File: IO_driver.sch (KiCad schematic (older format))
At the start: 9 parts, among them J2 BNC, U7 74LVC2T45DC

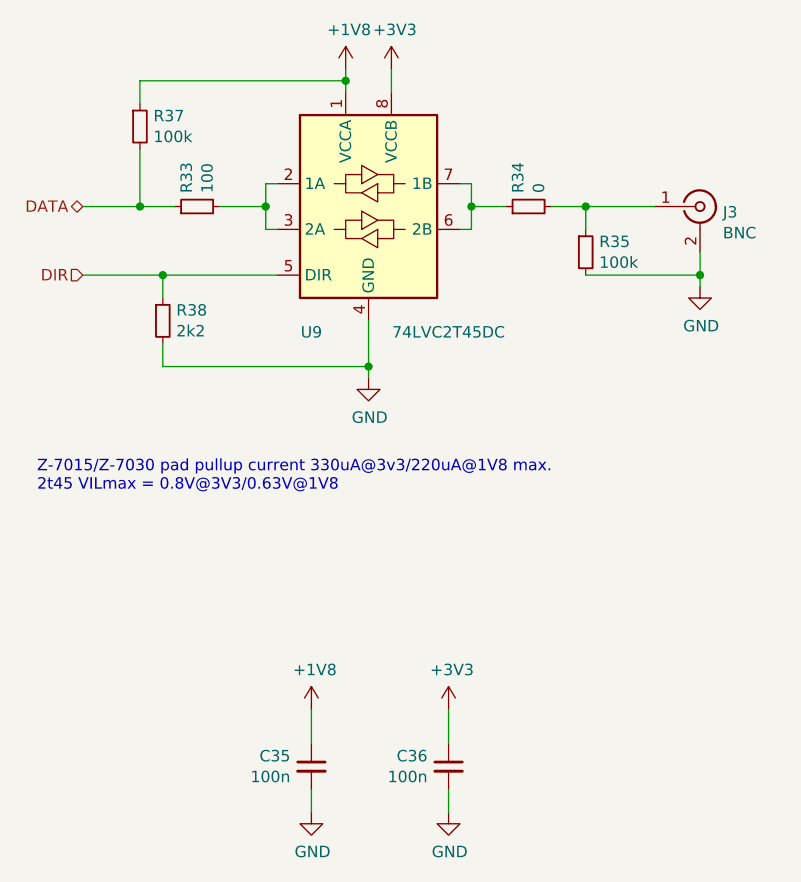
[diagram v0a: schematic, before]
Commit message: reannotated for merging with te0715 development board
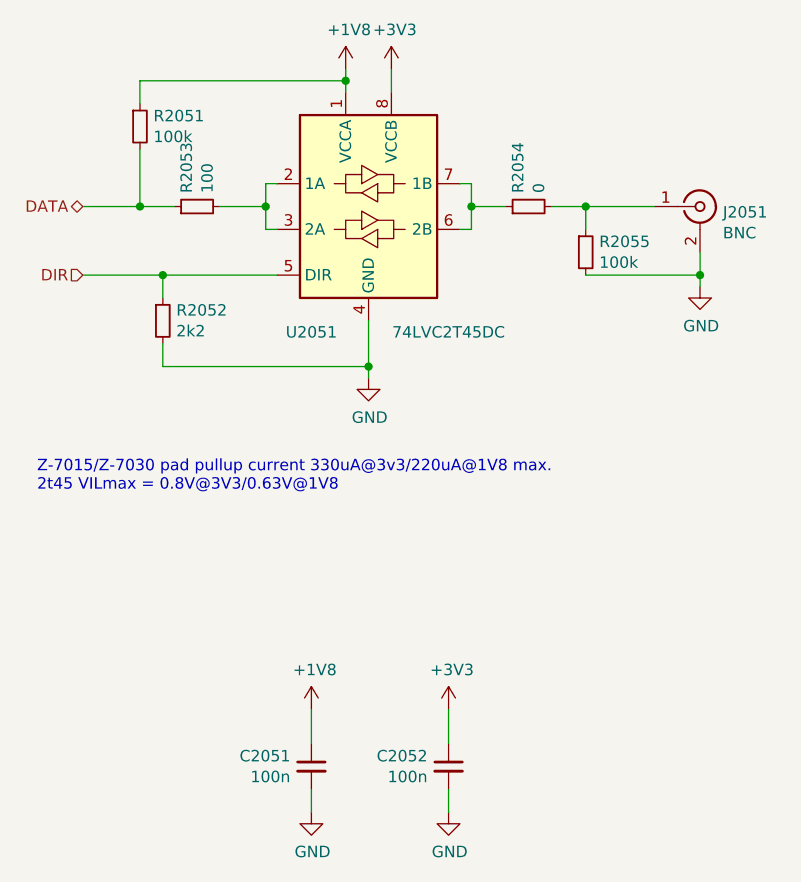
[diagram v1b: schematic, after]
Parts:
- renumbered C33 to C2001, C34 to C2002, J2 to J2001, R29 to R2001, R36 to R2002, R30 to R2003, R31 to R2004, R32 to R2005, U7 to U2001
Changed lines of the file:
@@
 $Descr A4 11693 8268
 encoding utf-8
-Sheet 5 6
+Sheet 6 6
 Title ""
 Date ""
@@
 AR Path="/60F26603" Ref="R?"  Part="1"
 AR Path="/60DB2574/60F26603" Ref="R?"  Part="1"
-AR Path="/60DB2574/60EF9F81/60F26603" Ref="R31"  Part="1"
-AR Path="/60DB2574/60E556C7/60F26603" Ref="R34"  Part="1"
-F 0 "R34" H 5259 1896 50  0000 L CNN
+AR Path="/60DB2574/60EF9F81/60F26603" Ref="R2004"  Part="1"
+AR Path="/60DB2574/60E556C7/60F26603" Ref="R2054"  Part="1"
+F 0 "R2054" H 5259 1896 50  0000 L CNN
 F 1 "0" H 5259 1805 50  0000 L CNN
 F 2 "Resistor_SMD:R_0603_1608Metric" H 5200 1850 50  0001 C CNN
@@
 AR Path="/60F26C82" Ref="R?"  Part="1"
 AR Path="/60DB2574/60F26C82" Ref="R?"  Part="1"
-AR Path="/60DB2574/60EF9F81/60F26C82" Ref="R30"  Part="1"
-AR Path="/60DB2574/60E556C7/60F26C82" Ref="R33"  Part="1"
-F 0 "R33" H 3809 1896 50  0000 L CNN
+AR Path="/60DB2574/60EF9F81/60F26C82" Ref="R2003"  Part="1"
+AR Path="/60DB2574/60E556C7/60F26C82" Ref="R2053"  Part="1"
+F 0 "R2053" H 3809 1896 50  0000 L CNN
 F 1 "100" H 3809 1805 50  0000 L CNN
 F 2 "Resistor_SMD:R_0603_1608Metric" H 3750 1850 50  0001 C CNN
@@
 	3250 2150 3600 2150
 $Comp
-L Device:C_Small C33
+L Device:C_Small C2001
 U 1 1 60F2A5CB
 P 4250 4300
-AR Path="/60DB2574/60EF9F81/60F2A5CB" Ref="C33"  Part="1"
-AR Path="/60DB2574/60E556C7/60F2A5CB" Ref="C35"  Part="1"
-F 0 "C35" H 4342 4346 50  0000 L CNN
+AR Path="/60DB2574/60EF9F81/60F2A5CB" Ref="C2001"  Part="1"
+AR Path="/60DB2574/60E556C7/60F2A5CB" Ref="C2051"  Part="1"
+F 0 "C2051" H 4342 4346 50  0000 L CNN
 F 1 "100n" H 4342 4255 50  0000 L CNN
 F 2 "Capacitor_SMD:C_0402_1005Metric" H 4250 4300 50  0001 C CNN
@@
 	4250 4400 4250 4500
 $Comp
-L Device:C_Small C34
+L Device:C_Small C2002
 U 1 1 60F2C544
 P 4850 4300
-AR Path="/60DB2574/60EF9F81/60F2C544" Ref="C34"  Part="1"
-AR Path="/60DB2574/60E556C7/60F2C544" Ref="C36"  Part="1"
-F 0 "C36" H 4942 4346 50  0000 L CNN
+AR Path="/60DB2574/60EF9F81/60F2C544" Ref="C2002"  Part="1"
+AR Path="/60DB2574/60E556C7/60F2C544" Ref="C2052"  Part="1"
+F 0 "C2052" H 4942 4346 50  0000 L CNN
 F 1 "100n" H 4942 4255 50  0000 L CNN
 F 2 "Capacitor_SMD:C_0402_1005Metric" H 4850 4300 50  0001 C CNN
@@
 AR Path="/612B1274/611783BC/60E51E93" Ref="J?"  Part="1"
 AR Path="/612B1274/611E90A8/60E51E93" Ref="J?"  Part="1"
-AR Path="/60DB2574/60EF9F81/60E51E93" Ref="J2"  Part="1"
-AR Path="/60DB2574/60E556C7/60E51E93" Ref="J3"  Part="1"
-F 0 "J3" H 6050 1825 50  0000 L CNN
+AR Path="/60DB2574/60EF9F81/60E51E93" Ref="J2001"  Part="1"
+AR Path="/60DB2574/60E556C7/60E51E93" Ref="J2051"  Part="1"
+F 0 "J2051" H 6050 1825 50  0000 L CNN
 F 1 "BNC" H 6050 1734 50  0000 L CNN
 F 2 "proj_footprints:BNC_Molex_0731713150" H 5950 1850 50  0001 C CNN
@@
 AR Path="/60F05839" Ref="R?"  Part="1"
 AR Path="/60DB2574/60F05839" Ref="R?"  Part="1"
-AR Path="/60DB2574/60EF9F81/60F05839" Ref="R32"  Part="1"
-AR Path="/60DB2574/60E556C7/60F05839" Ref="R35"  Part="1"
-F 0 "R35" H 5509 2096 50  0000 L CNN
+AR Path="/60DB2574/60EF9F81/60F05839" Ref="R2005"  Part="1"
+AR Path="/60DB2574/60E556C7/60F05839" Ref="R2055"  Part="1"
+F 0 "R2055" H 5509 2096 50  0000 L CNN
 F 1 "100k" H 5509 2005 50  0000 L CNN
 F 2 "Resistor_SMD:R_0603_1608Metric" H 5450 2050 50  0001 C CNN
@@
 Z-7015/Z-7030 pad pullup current 330uA@3v3/220uA@1V8 max.\n2t45 VILmax = 0.8V@3V3/0.63V@1V8
 $Comp
-L Logic_LevelTranslator:74LVC2T45DC U7
+L Logic_LevelTranslator:74LVC2T45DC U2001
 U 1 1 60E41AAA
 P 4500 1850
-AR Path="/60DB2574/60EF9F81/60E41AAA" Ref="U7"  Part="1"
-AR Path="/60DB2574/60E556C7/60E41AAA" Ref="U9"  Part="1"
-F 0 "U9" H 4250 1300 50  0000 C CNN
+AR Path="/60DB2574/60EF9F81/60E41AAA" Ref="U2001"  Part="1"
+AR Path="/60DB2574/60E556C7/60E41AAA" Ref="U2051"  Part="1"
+F 0 "U2051" H 4250 1300 50  0000 C CNN
 F 1 "74LVC2T45DC" H 4850 1300 50  0000 C CNN
 F 2 "Package_SO:VSSOP-8_2.3x2mm_P0.5mm" H 4500 1000 50  0001 C CNN
@@
 AR Path="/60E4921E" Ref="R?"  Part="1"
 AR Path="/60DB2574/60E4921E" Ref="R?"  Part="1"
-AR Path="/60DB2574/60EF9F81/60E4921E" Ref="R36"  Part="1"
-AR Path="/60DB2574/60E556C7/60E4921E" Ref="R38"  Part="1"
-F 0 "R38" H 3659 2396 50  0000 L CNN
+AR Path="/60DB2574/60EF9F81/60E4921E" Ref="R2002"  Part="1"
+AR Path="/60DB2574/60E556C7/60E4921E" Ref="R2052"  Part="1"
+F 0 "R2052" H 3659 2396 50  0000 L CNN
 F 1 "2k2" H 3659 2305 50  0000 L CNN
 F 2 "Resistor_SMD:R_0603_1608Metric" H 3600 2350 50  0001 C CNN
@@
 AR Path="/60E49E8E" Ref="R?"  Part="1"
 AR Path="/60DB2574/60E49E8E" Ref="R?"  Part="1"
-AR Path="/60DB2574/60EF9F81/60E49E8E" Ref="R29"  Part="1"
-AR Path="/60DB2574/60E556C7/60E49E8E" Ref="R37"  Part="1"
-F 0 "R37" H 3559 1546 50  0000 L CNN
+AR Path="/60DB2574/60EF9F81/60E49E8E" Ref="R2001"  Part="1"
+AR Path="/60DB2574/60E556C7/60E49E8E" Ref="R2051"  Part="1"
+F 0 "R2051" H 3559 1546 50  0000 L CNN
 F 1 "100k" H 3559 1455 50  0000 L CNN
 F 2 "Resistor_SMD:R_0603_1608Metric" H 3500 1500 50  0001 C CNN
